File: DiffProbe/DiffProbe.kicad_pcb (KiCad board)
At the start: 2 copper layers, 42.9 x 36 mm, 35 parts, among them J1 CONN_01X02, J2 BNC, J3 CONN_01X02, SW1 SPST, U1 LTC6268S6, U2 LTC6268S6, U3 LT1761

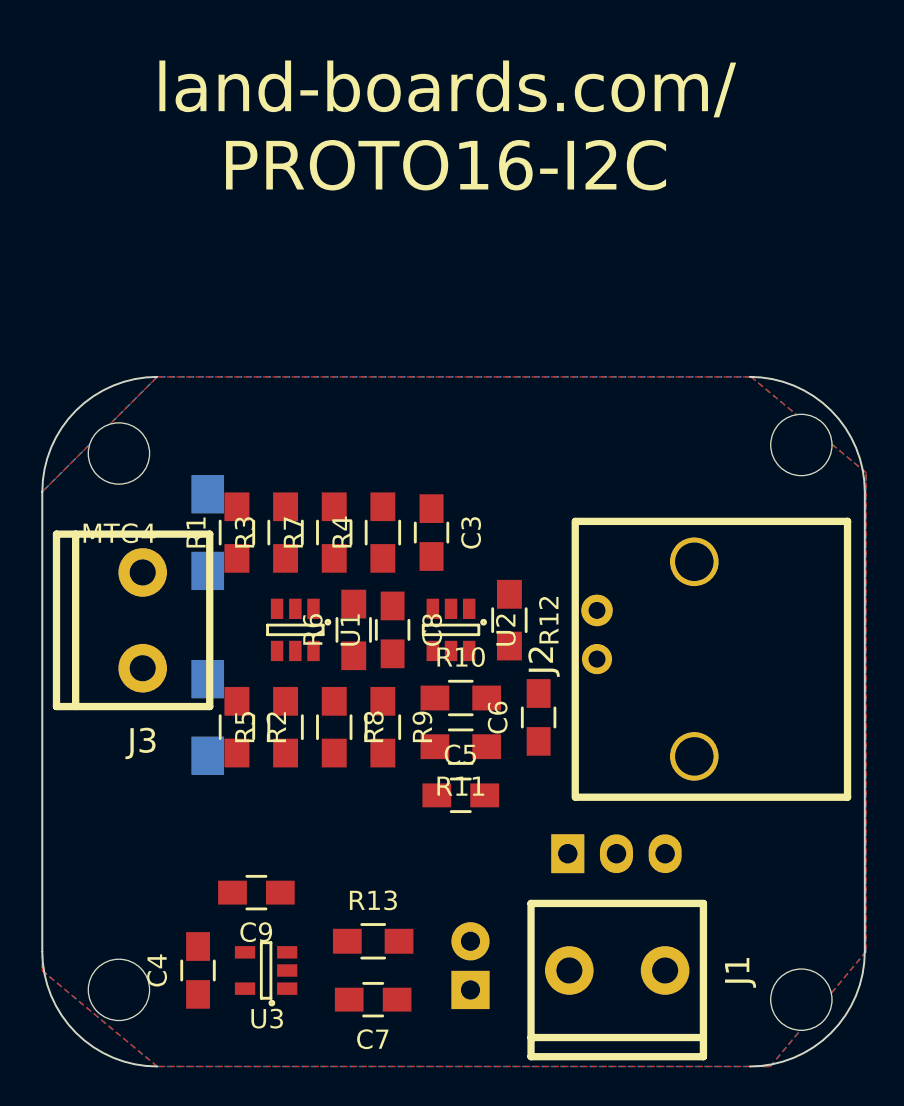
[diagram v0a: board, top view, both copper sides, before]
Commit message: Differential scope robe
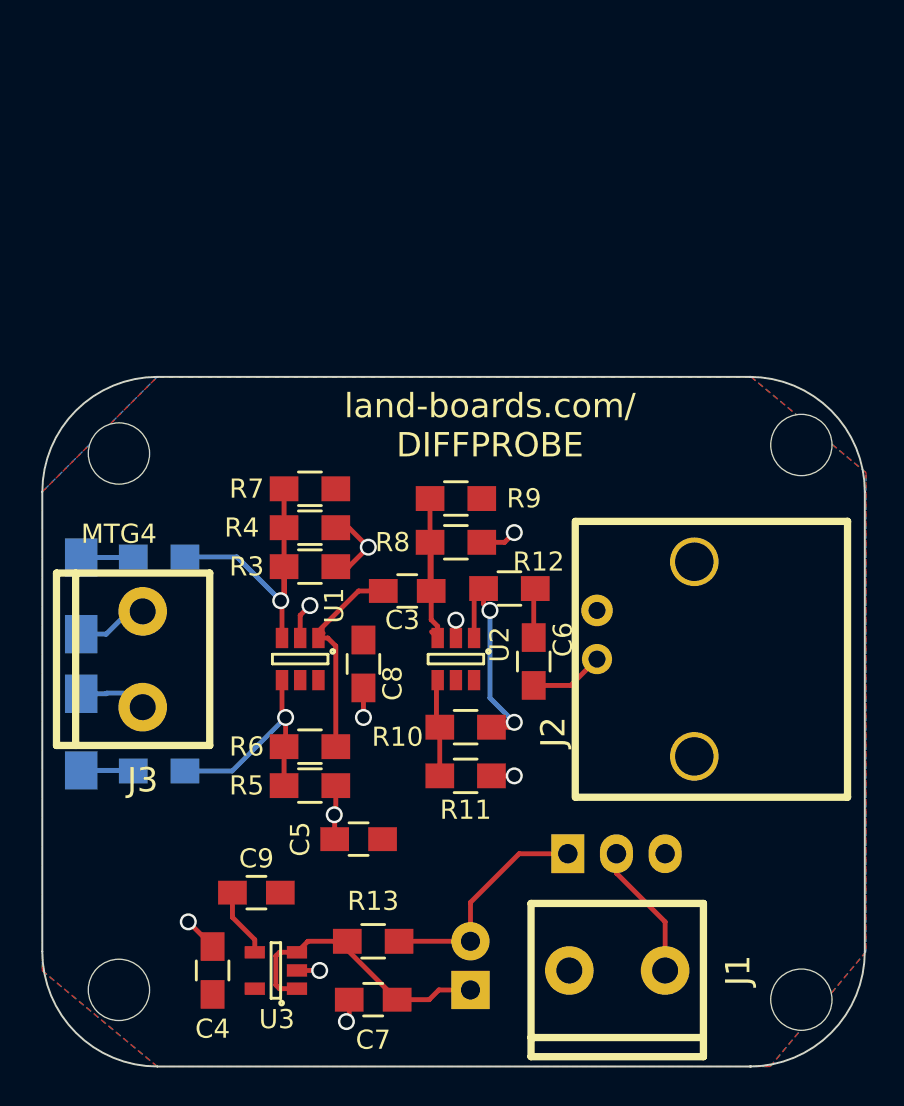
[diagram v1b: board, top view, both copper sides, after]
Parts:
- R1, R2: moved to B.Cu
- moved R9 12.5 mm to (21.6, 6.35), turned to 0 degrees
- moved R8 11.6 mm to (21.6, 8.64), turned to 0 degrees
- moved C1 7.38 mm to (2.03, 11.4)
- moved C2 6.65 mm to (2.03, 18.5)
- moved R6 6.51 mm to (14.0, 19.3), turned to 0 degrees
- moved C5 5.80 mm to (16.5, 24.1), turned to 180 degrees
- moved R2 4.66 mm to (6.10, 20.6), turned to 180 degrees
- moved R1 4.26 mm to (6.10, 9.40), turned to 180 degrees
- moved R4 3.82 mm to (14.0, 7.87), turned to 0 degrees
- moved C3 3.30 mm to (19.1, 11.2), turned to 180 degrees
- moved R5 3.30 mm to (14.0, 21.3), turned to 180 degrees
- moved C6 2.93 mm to (25.7, 14.9)
- moved R7 2.62 mm to (14.0, 5.84), turned to 0 degrees
- moved C8 2.34 mm to (16.8, 15.0)
- moved R3 2.18 mm to (14.0, 9.91), turned to 0 degrees
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- renumbered TESTED1 to TESTED
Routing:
- net GND: track 0.00 -> 18.8 mm, vias 0 -> 10
- net Net-(R1-Pad1): track 0.00 -> 16.0 mm, vias 0 -> 1
- net Net-(C7-Pad1): track 0.00 -> 14.9 mm
- net Net-(R2-Pad1): track 0.00 -> 12.3 mm, vias 0 -> 1
- net Net-(D1-Pad2): track 0.00 -> 11.9 mm
- net Net-(R10-Pad2): track 0.00 -> 11.7 mm, vias 0 -> 2
- net Net-(C3-Pad2): track 0.00 -> 11.4 mm
- net Net-(C3-Pad1): track 0.00 -> 10.5 mm
- net Net-(J1-Pad1): track 0.00 -> 7.15 mm
- net Net-(R10-Pad1): track 0.00 -> 5.10 mm
- net Net-(C2-Pad2): track 0.00 -> 4.33 mm
- net Net-(C6-Pad1): track 0.00 -> 3.87 mm
- net Net-(C1-Pad2): track 0.00 -> 3.82 mm
- net Net-(C9-Pad2): track 0.00 -> 3.60 mm
- net Net-(C2-Pad1): track 0.00 -> 2.73 mm
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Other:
- outline, holes or cut-outs redrawn
- board text added: "land-boards.com/ DIFFPROBE"
- board text removed: "land-boards.com/ PROTO16-I2C"

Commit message: Ordered a bunch of cards from seeedstudio
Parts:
- moved TESTED 4.44 mm to (38.1, 26.7)
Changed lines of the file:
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@@
-(kicad_pcb (version 4) (host pcbnew 4.0.1-stable)
+(kicad_pcb (version 4) (host pcbnew "(after 2015-mar-04 BZR unknown)-product")
   (general
     (links 51)
     (no_connects 0)
-    (area -10.999999 -7.85 48.847828 37.741)
+    (area -10.999999 -7.85 47.831828 37.741)
     (thickness 1.6)
     (drawings 12)
@@
     (pcbplotparams
       (layerselection 0x010f0_80000001)
-      (usegerberextensions true)
+      (usegerberextensions false)
       (excludeedgelayer true)
       (linewidth 0.150000)
@@
     (tags "resistor 1206")
     (attr smd)
-    (fp_text reference C1 (at 0 2.3 270) (layer B.SilkS)
+    (fp_text reference C1 (at -3.81 0.127 360) (layer B.SilkS)
       (effects (font (size 1 1) (thickness 0.15)) (justify mirror))
     )
@@
     (tags "resistor 0805")
     (attr smd)
-    (fp_text reference R1 (at 0 2.1 180) (layer B.SilkS)
+    (fp_text reference R1 (at -0.254 1.778 180) (layer B.SilkS)
       (effects (font (size 1 1) (thickness 0.15)) (justify mirror))
     )
@@
   )
   (module DougsNewMods:TEST_BLK-REAR (layer F.Cu)
-    (at 39.116 22.352)
+    (at 38.1 26.67)
     (fp_text reference TESTED (at 0 -3.5) (layer B.SilkS)
       (effects (font (thickness 0.3048)) (justify mirror))
